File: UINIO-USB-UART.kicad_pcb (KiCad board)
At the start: 2 copper layers, 72.2 x 20.5 mm, 48 parts, among them J1 Conn_01x08_Male, J2 Conn_01x04_Male, J3 Conn_01x07_Male, J4 Conn_01x06_Male, J5 Conn_01x04_Male, J6 Conn_01x07_Male, J7 Conn_01x03_Male, U1 CP2102, U2 CH343P

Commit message: Release UINIO-USB-UART version 3.0.0.
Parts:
- moved C5 0.38 mm to (142.6, 104.0)
- moved ? 0.11 mm to (187.4, 99.9)
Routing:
- net GND: track 202.5 -> 208.2 mm, vias 37 -> 40
- net /CP2102_VDD_5V: track 44.6 -> 46.8 mm
- net /CH343_VDD_5V: track 58.6 -> 57.7 mm
- net /CH343_VIO: track 46.3 -> 47.3 mm
- net /CP2102_DTR: track 28.1 -> 27.4 mm
- net /CH343_RXD: track 26.5 -> 27.1 mm

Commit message: Release UINIO-USB-UART version 3.0.0.
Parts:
- moved ? 0.08 mm to (133.8, 99.9)
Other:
- board text added: "CH343"
- board text removed: "CH343P"

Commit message: Update PCB.
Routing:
- net GND: vias 40 -> 41
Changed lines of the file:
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@@
   (via (at 183.32 93.35) (size 0.5) (drill 0.3) (layers "F.Cu" "B.Cu") (free) (net 2))
   (via (at 142.23 99.79) (size 0.5) (drill 0.3) (layers "F.Cu" "B.Cu") (net 2))
+  (via (at 178.29 106.89) (size 0.5) (drill 0.3) (layers "F.Cu" "B.Cu") (free) (net 2))
   (via (at 137.27 95.4) (size 0.7) (drill 0.4) (layers "F.Cu" "B.Cu") (free) (net 2))
   (via (at 142.95 100.49) (size 0.5) (drill 0.3) (layers "F.Cu" "B.Cu") (net 2))

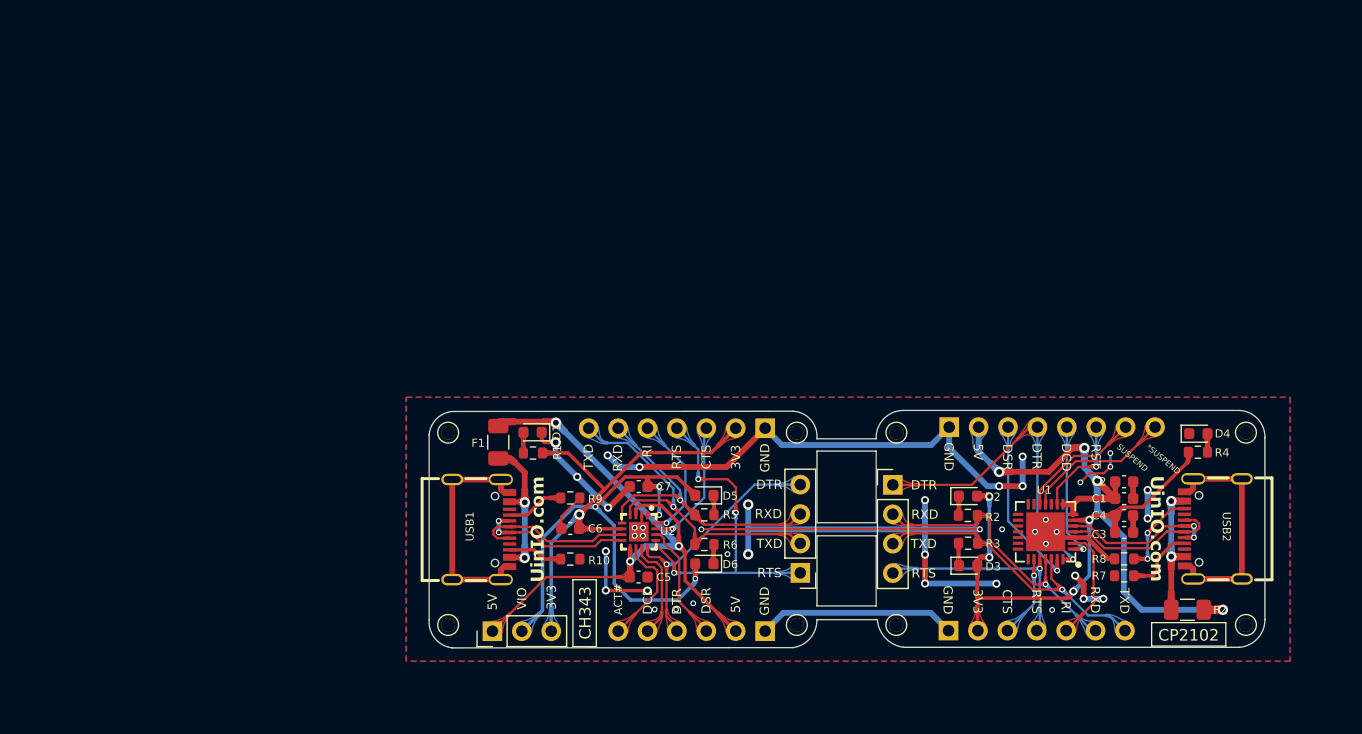
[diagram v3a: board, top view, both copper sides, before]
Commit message: Prepare UINIO-USB-UART version 3.1.0
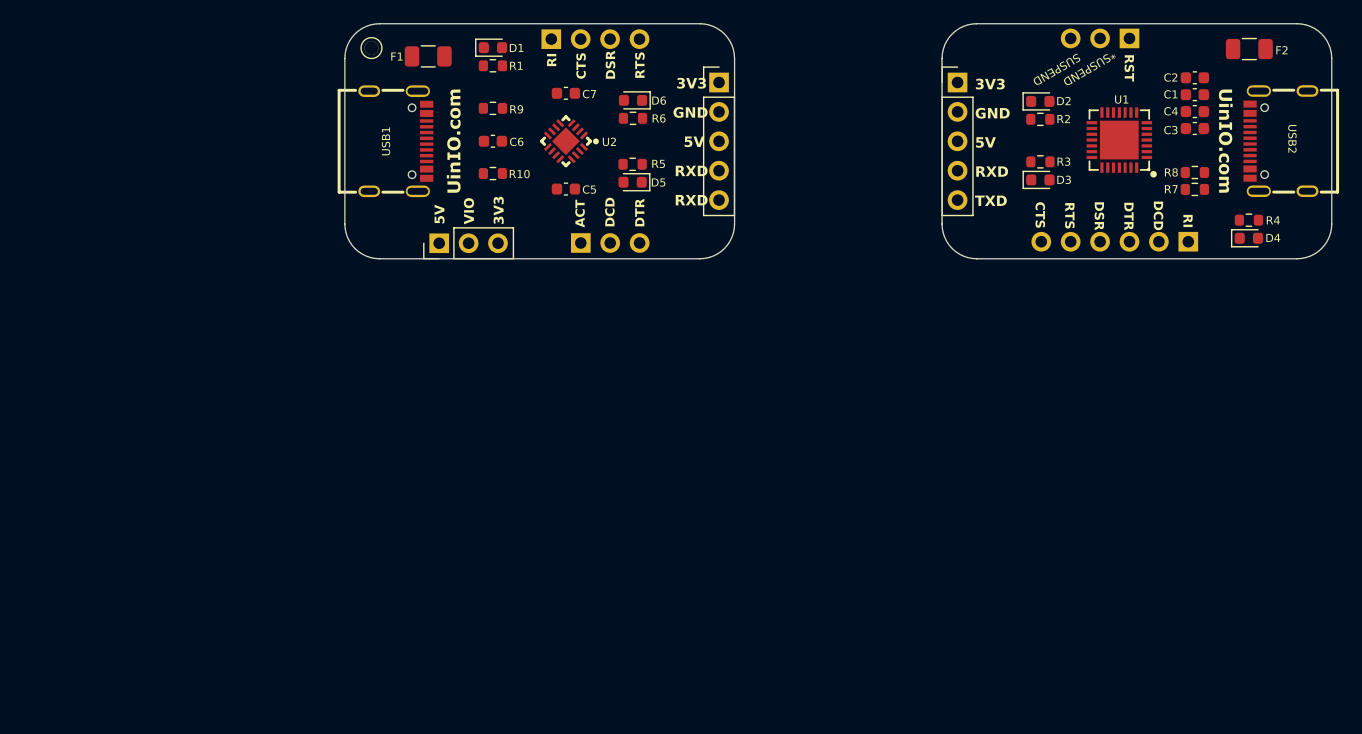
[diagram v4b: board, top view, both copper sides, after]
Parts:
- removed Hole1, Hole2, Hole3, Hole4, Hole5, Hole6, Hole7, Hole8: Hole-1mm, Uinio:Hole-1mm
- added HOLE**: Hole-1mm, Uinio:Hole-1mm, F.Cu at (119.5, 58.4)
- J1: value Conn_01x08_Male -> Conn_01x03_Pin; footprint Connector_PinHeader_2.54mm:PinHeader_1x08_P2.54mm_Vertical -> Connector_PinHeader_2.54mm:PinHeader_1x03_P2.54mm_Vertical
- J2, J5: value Conn_01x04_Male -> Conn_01x05_Pin; footprint Connector_PinHeader_2.54mm:PinHeader_1x04_P2.54mm_Vertical -> Connector_PinHeader_2.54mm:PinHeader_1x05_P2.54mm_Vertical
- J3: value Conn_01x07_Male -> Conn_01x06_Pin; footprint Connector_PinHeader_2.54mm:PinHeader_1x07_P2.54mm_Vertical -> Connector_PinHeader_2.54mm:PinHeader_1x06_P2.54mm_Vertical
- J4: value Conn_01x06_Male -> Conn_01x03_Pin; footprint Connector_PinHeader_2.54mm:PinHeader_1x06_P2.54mm_Vertical -> Connector_PinHeader_2.54mm:PinHeader_1x03_P2.54mm_Vertical
- J6: value Conn_01x07_Male -> Conn_01x04_Pin; footprint Connector_PinHeader_2.54mm:PinHeader_1x07_P2.54mm_Vertical -> Connector_PinHeader_2.54mm:PinHeader_1x04_P2.54mm_Vertical
- moved F2 48.7 mm to (195.3, 58.5), turned to 180 degrees
- moved J5 42.9 mm to (149.5, 61.3), turned to 0 degrees
- moved D6 40.5 mm to (142.1, 62.9)
- moved J3 39.5 mm to (190.1, 75.1), turned to 90 degrees
- moved J6 38.3 mm to (135.0, 57.6), turned to -90 degrees
- moved R6 37.3 mm to (142.1, 64.4)
- moved J4 37.1 mm to (137.6, 75.2), turned to -90 degrees
- moved J1 37.0 mm to (185.0, 57.5), turned to 90 degrees
- moved C1 35.4 mm to (190.6, 62.4)
- moved C3 35.4 mm to (190.6, 65.3)
- moved C2 35.4 mm to (190.6, 60.9)
- moved C4 35.4 mm to (190.6, 63.9)
- moved J2 35.2 mm to (170.1, 61.3)
- moved R2 34.8 mm to (177.3, 64.5)
- moved D2 34.7 mm to (177.3, 63.0)
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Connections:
- J1 pad 1: GND -> /CP2102_RST
- J1 pad 2: /CP2102_VDD_5V -> /CP2102_*SUSPEND
- J1 pad 3: /CP2102_DSR -> /CP2102_SUSPEND
- J2 pad 1: /CP2102_DTR -> /CP2102_VDD_3.3V
- J2 pad 2: /CP2102_RXD -> GND
- J2 pad 3: /CP2102_TXD -> /CP2102_VDD_5V
- J2 pad 4: /CP2102_RTS -> /CP2102_RXD
- J3 pad 1: GND -> /CP2102_RI
- J3 pad 2: /CP2102_VDD_3.3V -> /CP2102_DCD
- J3 pad 3: /CP2102_CTS -> /CP2102_DTR
- J3 pad 4: /CP2102_RTS -> /CP2102_DSR
- J3 pad 5: /CP2102_RI -> /CP2102_RTS
- J3 pad 6: /CP2102_RXD -> /CP2102_CTS
- J4 pad 1: GND -> /CH343_ACT#
- J4 pad 2: /CH343_VDD_5V -> /CH343_DCD
- J4 pad 3: /CH343_DSR -> /CH343_DTR
- J5 pad 1: /CH343_RTS -> /CH343_VDD_5V
- J5 pad 2: /CH343_TXD -> GND
- J5 pad 3: /CH343_RXD -> /CH343_VDD_3.3V
- J5 pad 4: /CH343_DTR -> /CH343_RXD
- J6 pad 1: GND -> /CH343_RI
- J6 pad 2: /CH343_VDD_3.3V -> /CH343_CTS
- J6 pad 3: /CH343_CTS -> /CH343_DSR
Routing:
- net GND: track 208.2 -> 0.00 mm, vias 41 -> 0
- net /CH343_VDD_5V: track 57.7 -> 0.00 mm, vias 3 -> 0
- net /CH343_VIO: track 47.3 -> 0.00 mm, vias 4 -> 0
- net /CP2102_VDD_5V: track 46.8 -> 0.00 mm, vias 4 -> 0
- net /CP2102_VDD_3.3V: track 44.3 -> 0.00 mm, vias 4 -> 0
- net /CH343_VDD_3.3V: track 40.4 -> 0.00 mm, vias 1 -> 0
- net /CH343_RTS: track 30.5 -> 0.00 mm, vias 3 -> 0
- net /CH343_TXD: track 29.7 -> 0.00 mm, vias 1 -> 0
- net /CP2102_DTR: track 27.4 -> 0.00 mm, vias 1 -> 0
- net /CP2102_TXD: track 27.2 -> 0.00 mm, vias 1 -> 0
- net /CH343_RXD: track 27.1 -> 0.00 mm, vias 1 -> 0
- net /CP2102_RXD: track 26.0 -> 0.00 mm, vias 1 -> 0
- net /CH343_DTR: track 22.6 -> 0.00 mm, vias 1 -> 0
- net /CP2102_RTS: track 18.2 -> 0.00 mm, vias 1 -> 0
- net /CP2102_DSR: track 15.1 -> 0.00 mm, vias 1 -> 0
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- removed copper zone on B.Cu, net GND
- removed copper zone on F.Cu, net GND
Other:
- board size 72.2 x 20.5 mm -> 85.2 x 20.3 mm
- board text added: "ACT"
- board text removed: "ACT#"
- board text removed: "CH343"
- board text removed: "CP2102"
- board text removed: "UINIO-USB-UART-CH343"
- board text removed: "UINIO-USB-UART-CP2102"
- board text removed: "Version 3.0.0"

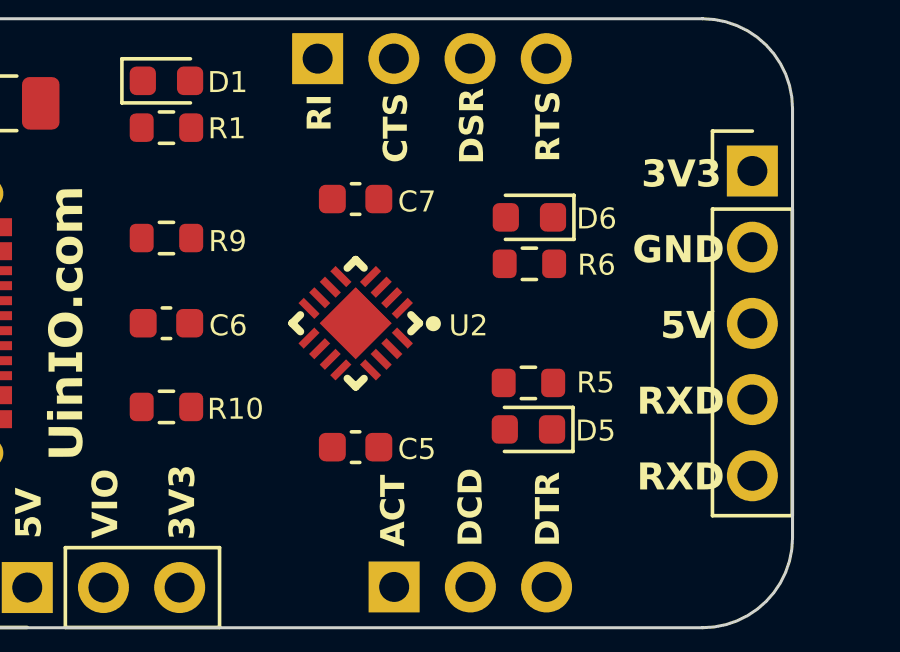
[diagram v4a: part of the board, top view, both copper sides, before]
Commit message: Prepare UINIO-USB-UART version 3.1.0
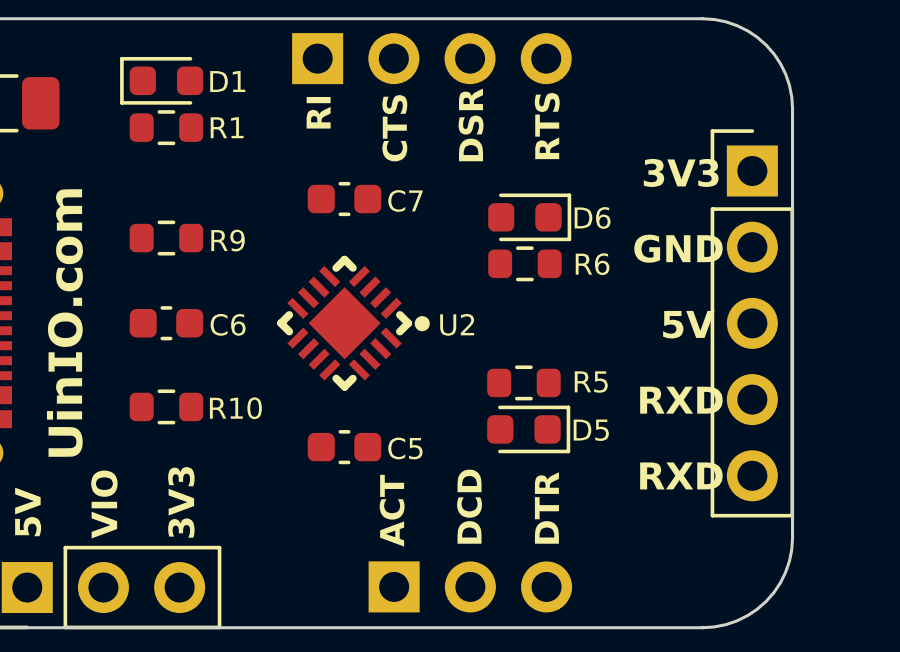
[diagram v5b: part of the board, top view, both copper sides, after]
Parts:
- moved C5 0.37 mm to (135.9, 70.5)
- moved C7 0.37 mm to (135.9, 62.3)
- moved U2 0.37 mm to (135.9, 66.4)
- moved D5 0.15 mm to (141.9, 70.0)
- moved D6 0.15 mm to (141.9, 62.9)
- moved R5 0.15 mm to (141.9, 68.4)
- moved R6 0.15 mm to (141.9, 64.4)

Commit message: Prepare Version 3.2.0.
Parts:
- added HOLE**: Hole-1mm, Uinio:Hole-1mm, F.Cu at (92.6, 67.4)
- added HOLE**: Hole-1mm, Uinio:Hole-1mm, F.Cu at (121.9, 111.7)
- added HOLE**: Hole-1mm, Uinio:Hole-1mm, F.Cu at (121.9, 83.3)
- added HOLE**: Hole-1mm, Uinio:Hole-1mm, F.Cu at (121.9, 67.4)
- added HOLE**: Hole-1mm, Uinio:Hole-1mm, F.Cu at (92.6, 83.3)
- added HOLE**: Hole-1mm, Uinio:Hole-1mm, F.Cu at (92.6, 111.7)
- added HOLE**: Hole-1mm, Uinio:Hole-1mm, F.Cu at (121.9, 95.8)
- J7: value Conn_01x03_Male -> Conn_01x03_Pin
- moved USB2 103.6 mm to (94.6, 75.4), turned to -90 degrees
- moved F2 100.4 mm to (97.9, 82.8), turned to 0 degrees
- moved D4 98.0 mm to (97.6, 67.0), turned to 180 degrees
- moved R4 97.8 mm to (97.6, 68.5), turned to 0 degrees
- moved ? 94.4 mm to (99.3, 75.4), turned to 90 degrees
- moved C2 90.6 mm to (102.3, 80.8), turned to 180 degrees
- moved C1 90.0 mm to (102.3, 79.4), turned to 180 degrees
- moved C4 89.5 mm to (102.3, 77.9), turned to 180 degrees
- moved C3 89.0 mm to (102.3, 76.5), turned to 180 degrees
- moved R8 88.4 mm to (102.3, 72.7), turned to 180 degrees
- moved R7 88.3 mm to (102.3, 71.2), turned to 180 degrees
- moved J3 87.6 mm to (102.8, 66.7), turned to -90 degrees
- moved J1 81.5 mm to (107.9, 84.2), turned to -90 degrees
- moved U1 75.9 mm to (108.8, 75.5), turned to 0 degrees
- moved ? 74.7 mm to (232.2, 112.0)
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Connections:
- J2 pad 1: /CP2102_VDD_3.3V -> /CP2102_VDD_5V
- J2 pad 3: /CP2102_VDD_5V -> /CP2102_VDD_3.3V
- J5 pad 4: /CH343_RXD -> /CH343_TXD
- J5 pad 5: /CH343_TXD -> /CH343_RXD
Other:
- board size 85.2 x 20.3 mm -> 33.7 x 48.7 mm
- board text added: "CH343P"
- board text added: "CP2102"
- board text added: "UINIO-USB-UART-CH343P"
- board text added: "UINIO-USB-UART-CP2102"
- board text added: "Version 3.2.0"

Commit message: Update PCB.
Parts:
- removed the ? at (232.2, 112.0)
- removed the ? at (210.4, 111.9)
- added ?: LOGO, LOGO, F.Cu at (144.1, 107.4)
- added ?: LOGO, LOGO, F.Cu at (128.1, 107.4)
- added ?: LOGO, LOGO, F.Cu at (172.5, 107.3)
- added ?: LOGO, LOGO, F.Cu at (156.6, 106.3)
- added ?: LOGO, LOGO, B.Cu at (136.1, 97.2)
- added ?: LOGO, LOGO, B.Cu at (164.5, 97.2)
- moved HOLE** 81.0 mm to (172.5, 81.0), turned to -90 degrees
- moved D4 77.3 mm to (172.5, 86.0), turned to 90 degrees
- moved R4 75.4 mm to (171.0, 86.0), turned to -90 degrees
- moved J3 74.5 mm to (173.2, 91.3), turned to 180 degrees
- moved USB2 70.3 mm to (164.5, 83.0), turned to 180 degrees
- moved R7 69.2 mm to (168.7, 90.7), turned to 90 degrees
- moved R8 67.4 mm to (167.2, 90.7), turned to 90 degrees
- moved HOLE** 66.3 mm to (172.5, 110.3), turned to 180 degrees
- moved ? 66.3 mm to (164.5, 87.7), turned to 0 degrees
- moved HOLE** 63.9 mm to (156.5, 81.1), turned to 0 degrees
- moved C4 62.4 mm to (163.4, 90.7), turned to 90 degrees
- moved C3 61.3 mm to (161.9, 90.7), turned to 90 degrees
- moved D3 61.3 mm to (167.8, 104.0), turned to 90 degrees
- moved U1 59.7 mm to (164.4, 97.2), turned to -90 degrees
- moved C1 59.3 mm to (160.5, 90.7), turned to 90 degrees
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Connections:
- J7 pad 1: /CH343_VDD_5V -> /CH343_VDD_3.3V
- J7 pad 3: /CH343_VDD_3.3V -> /CH343_VDD_5V
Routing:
- net GND: track 0.00 -> 82.6 mm, vias 0 -> 29
- net /CH343_VDD_5V: track 0.00 -> 72.2 mm, vias 0 -> 3
- net /CP2102_VDD_3.3V: track 0.00 -> 49.6 mm, vias 0 -> 4
- net /CH343_VDD_3.3V: track 0.00 -> 45.4 mm, vias 0 -> 2
- net /CP2102_VDD_5V: track 0.00 -> 34.1 mm, vias 0 -> 1
- net /CH343_VIO: track 0.00 -> 30.3 mm, vias 0 -> 3
- net /CP2102_RXD: track 0.00 -> 21.8 mm
- net /CH343_RTS: track 0.00 -> 21.4 mm, vias 0 -> 1
- net /CH343_DSR: track 0.00 -> 20.2 mm, vias 0 -> 1
- net /CH343_CTS: track 0.00 -> 19.4 mm, vias 0 -> 1
- net /CH343_TXD: track 0.00 -> 19.3 mm
- net /CP2102_TXD: track 0.00 -> 19.2 mm
- net /CH343_RI: track 0.00 -> 17.7 mm, vias 0 -> 1
- net /CH343_RXD: track 0.00 -> 16.6 mm
- net /CH343_USB_Data_P: track 0.00 -> 15.1 mm
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- added copper zone on B.Cu, net GND
- added copper zone on F.Cu, net GND
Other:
- board size 33.7 x 48.7 mm -> 48.7 x 33.7 mm

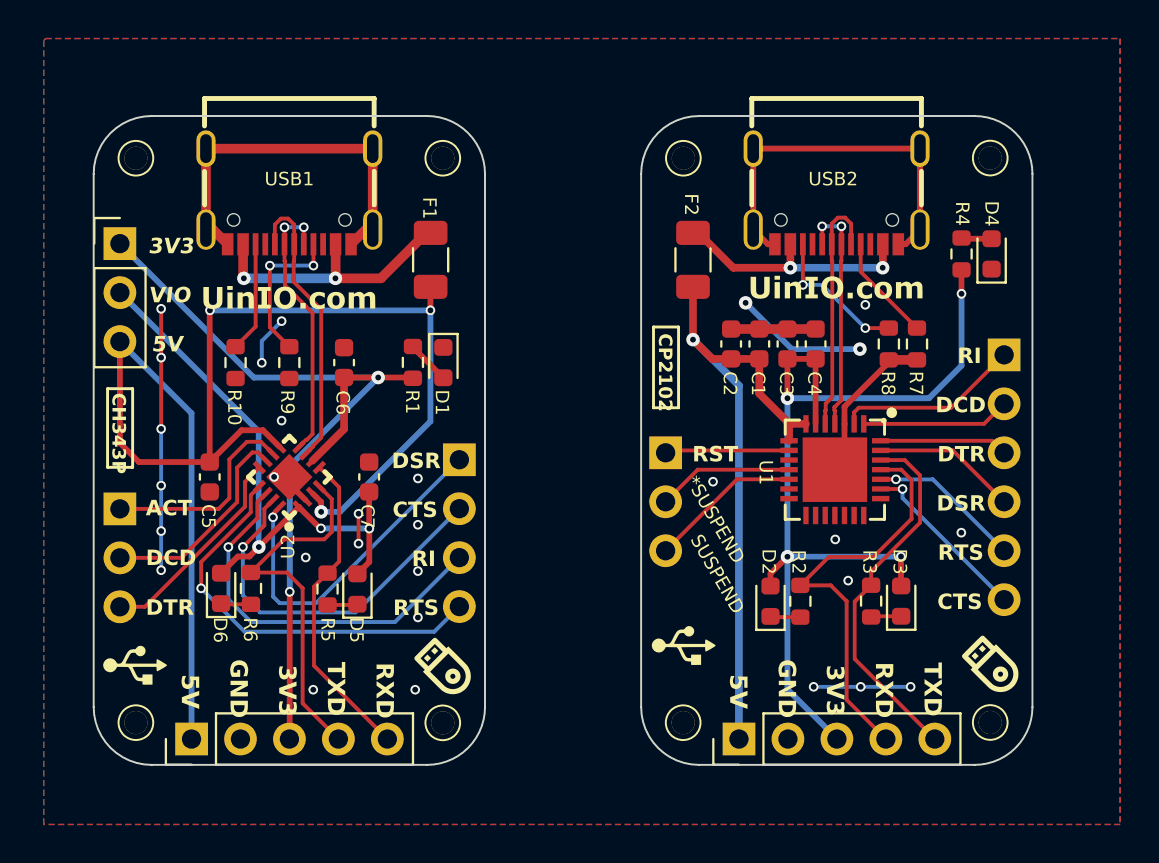
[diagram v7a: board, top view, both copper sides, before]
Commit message: Prepare UINIO-USB-UART Version 3.2.0
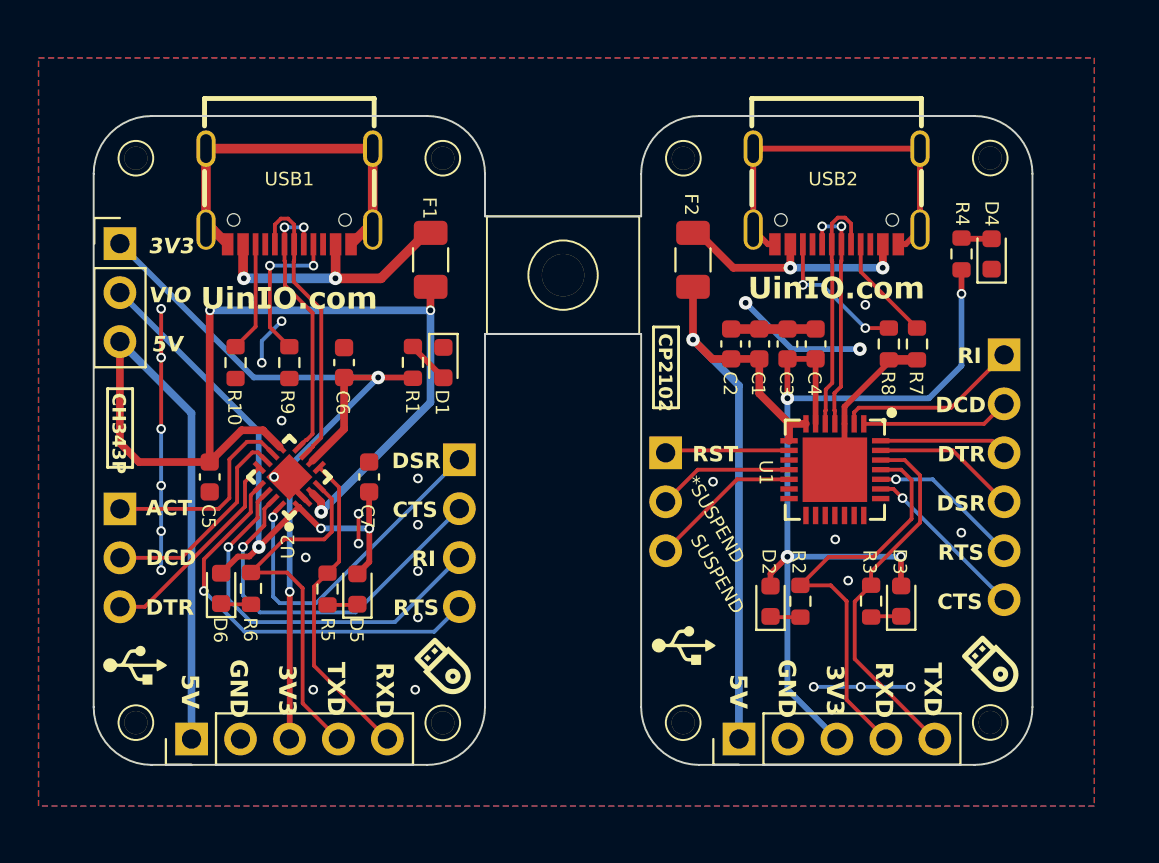
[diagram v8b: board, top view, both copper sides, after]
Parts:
- added HOLE**: Hole-2mm, Uinio:Hole-2mm, F.Cu at (150.3, 87.1)
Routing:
- net /CH343_VDD_5V: track 72.2 -> 71.6 mm
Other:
- outline, holes or cut-outs redrawn
